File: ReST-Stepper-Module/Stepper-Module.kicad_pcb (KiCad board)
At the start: 2 copper layers, 46 x 32.2 mm, 13 parts, among them P1 CONN_02X10, P2 CONN_01X04, P3 CONN_01X04, P4 CONN_01X04, P5 CONN_01X04, P6 CONN_02X03, P7 CONN_02X03, U1 POLOLU_A4988, U2 POLOLU_A4988

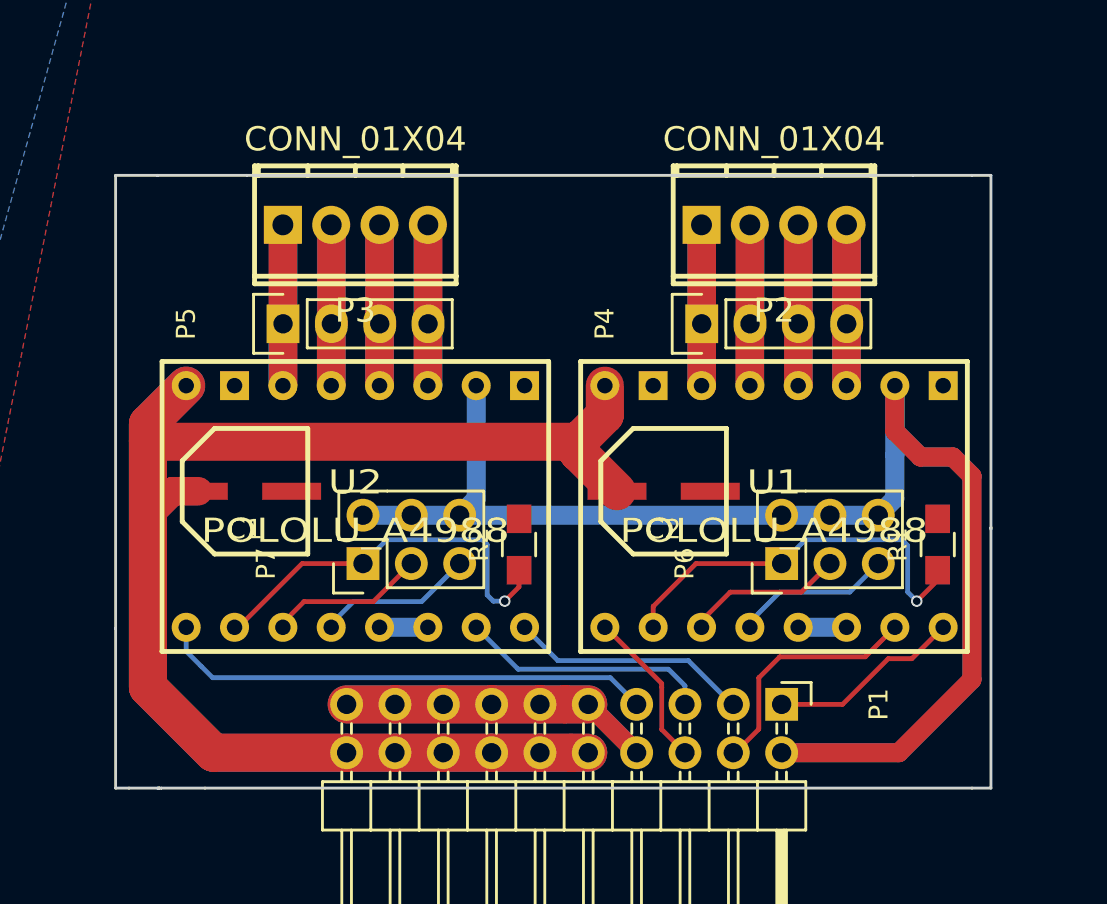
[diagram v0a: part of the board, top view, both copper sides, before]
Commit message: Added Images and PDF's
+ Silkscreening
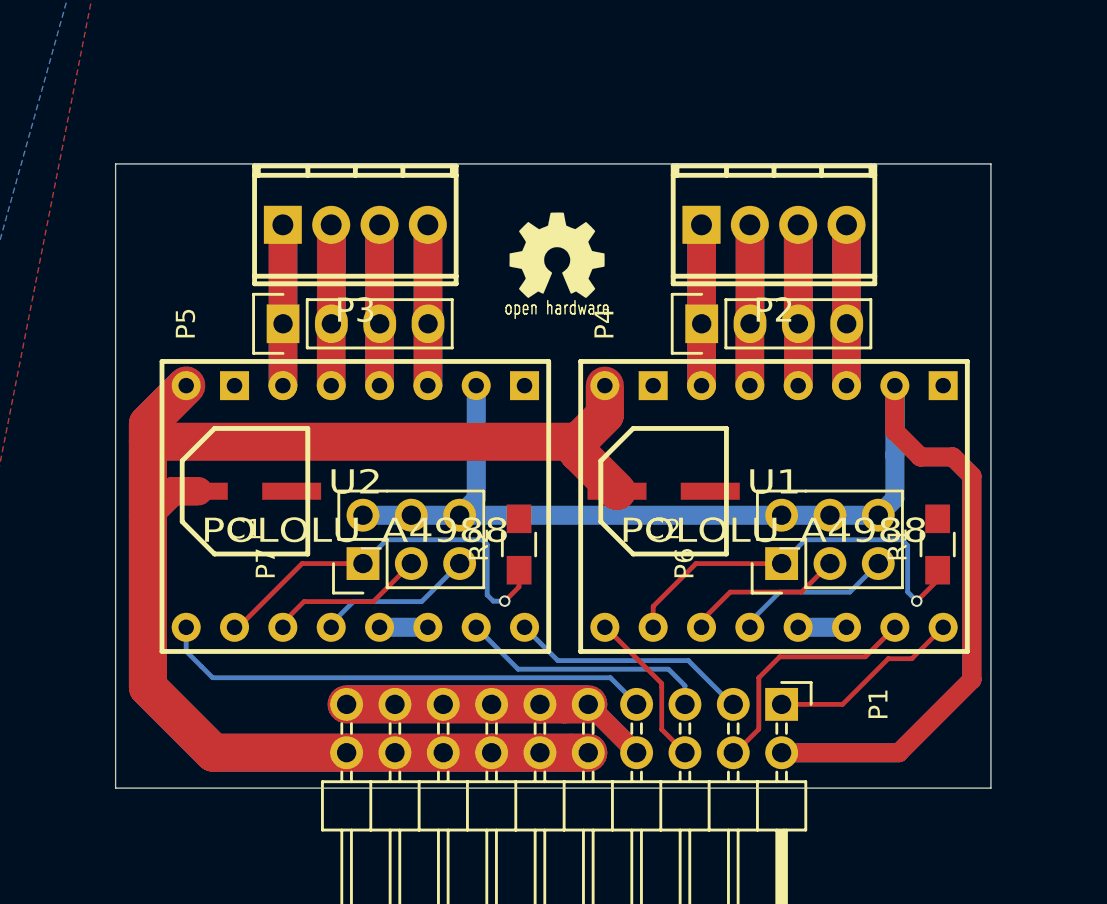
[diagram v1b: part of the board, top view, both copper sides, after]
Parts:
- added G***: LOGO, ReST-Library:STM32, B.Cu at (125.2, 83.6)
- added G***: LOGO, ReST-Library:Logo_silk_OSHW_6x6mm, F.Cu at (125.6, 82.8)
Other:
- board size 46 x 32.2 mm -> 46 x 32.8 mm
- board text added: "ReST32 Stepper Module Rev. A | Test by Straw"

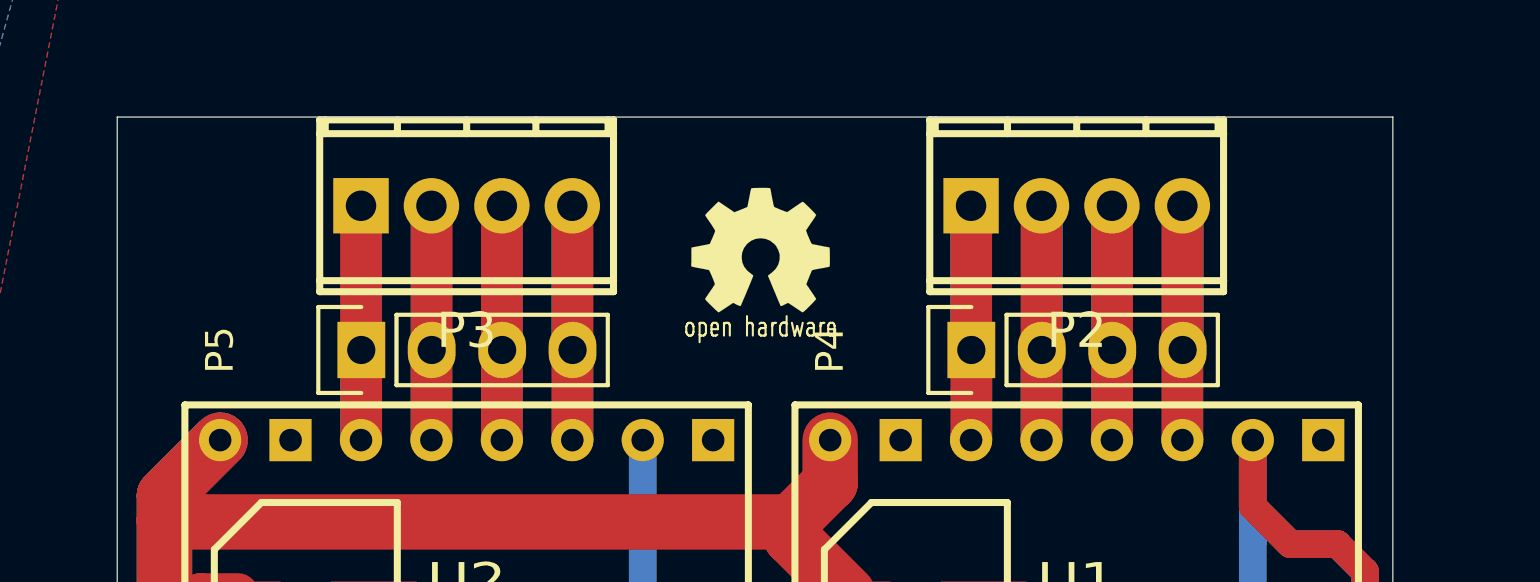
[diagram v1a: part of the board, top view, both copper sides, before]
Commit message: Added Mounting Holes to all Modules
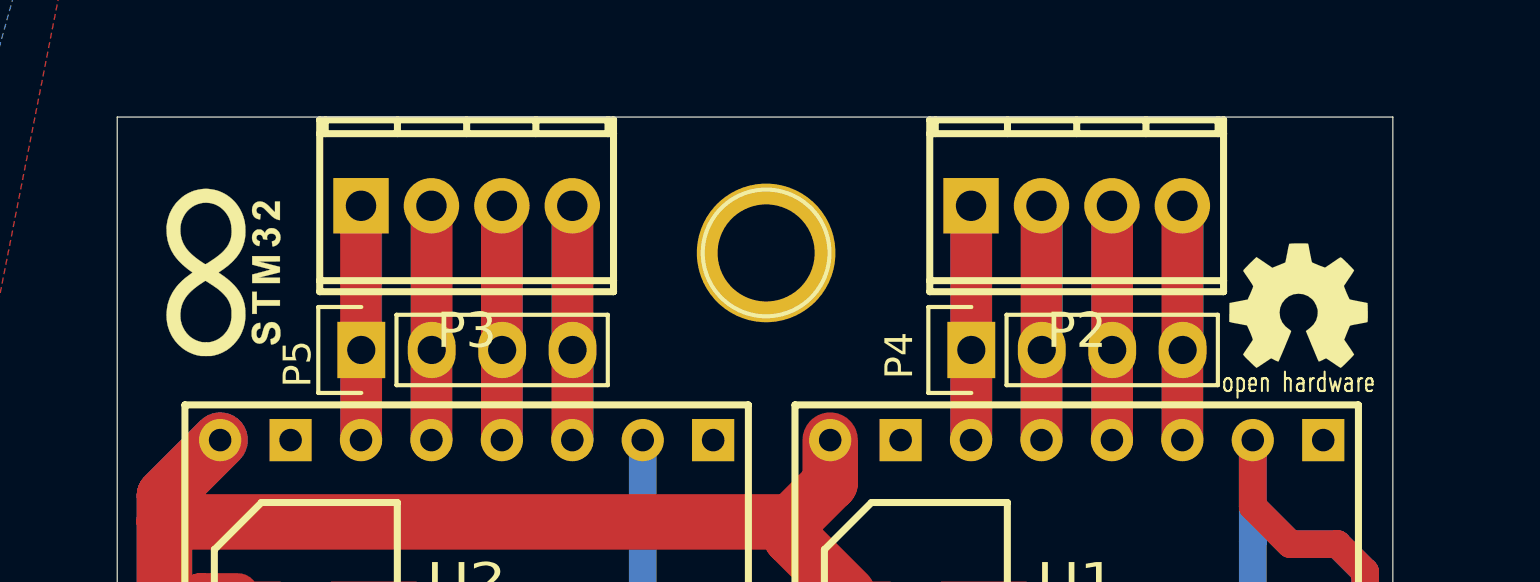
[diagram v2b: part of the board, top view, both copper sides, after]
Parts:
- added ?: 1pin, Connect:1pin, F.Cu at (125.8, 82.9)
- G***: moved to F.Cu
- moved G*** 19.5 mm to (145.0, 84.8)
- moved G*** 18.9 mm to (106.3, 83.6), turned to 90 degrees

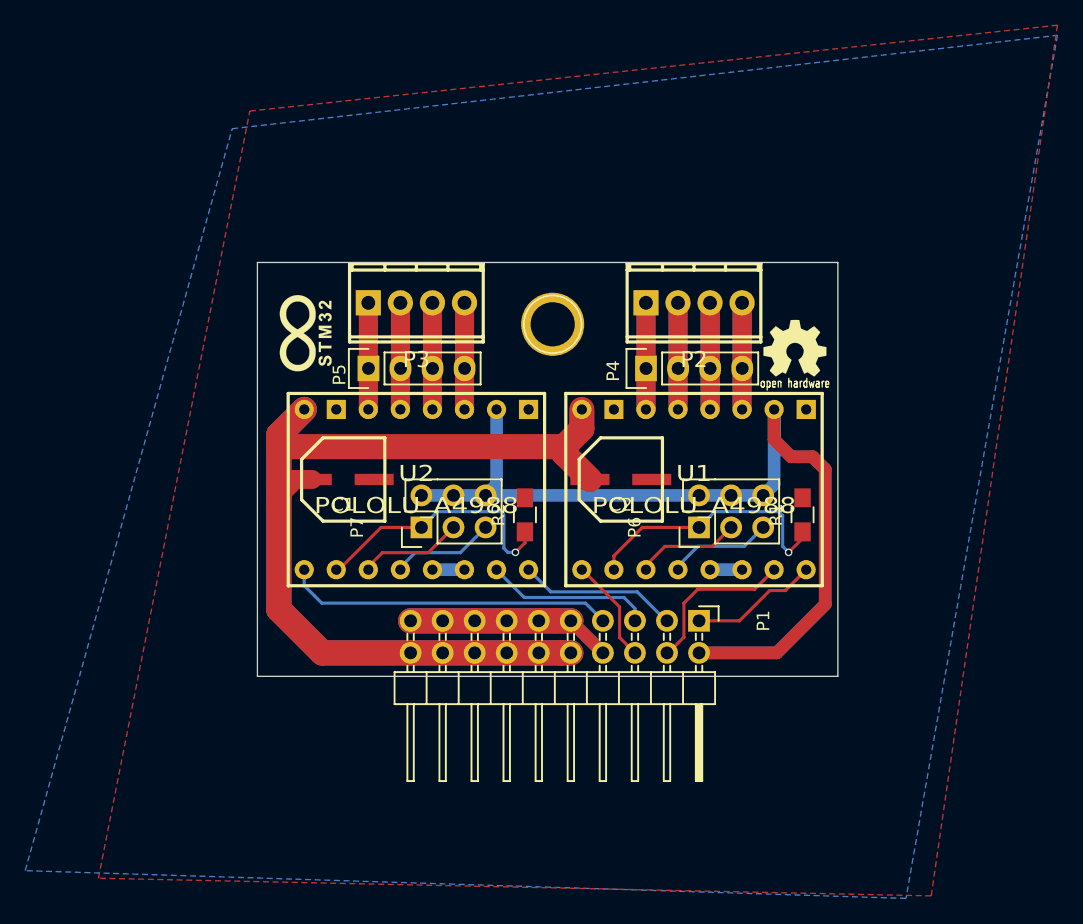
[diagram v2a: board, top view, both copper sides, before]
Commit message: Finally removed all unnecessary Libs and added Heatsink for 5V Regulator
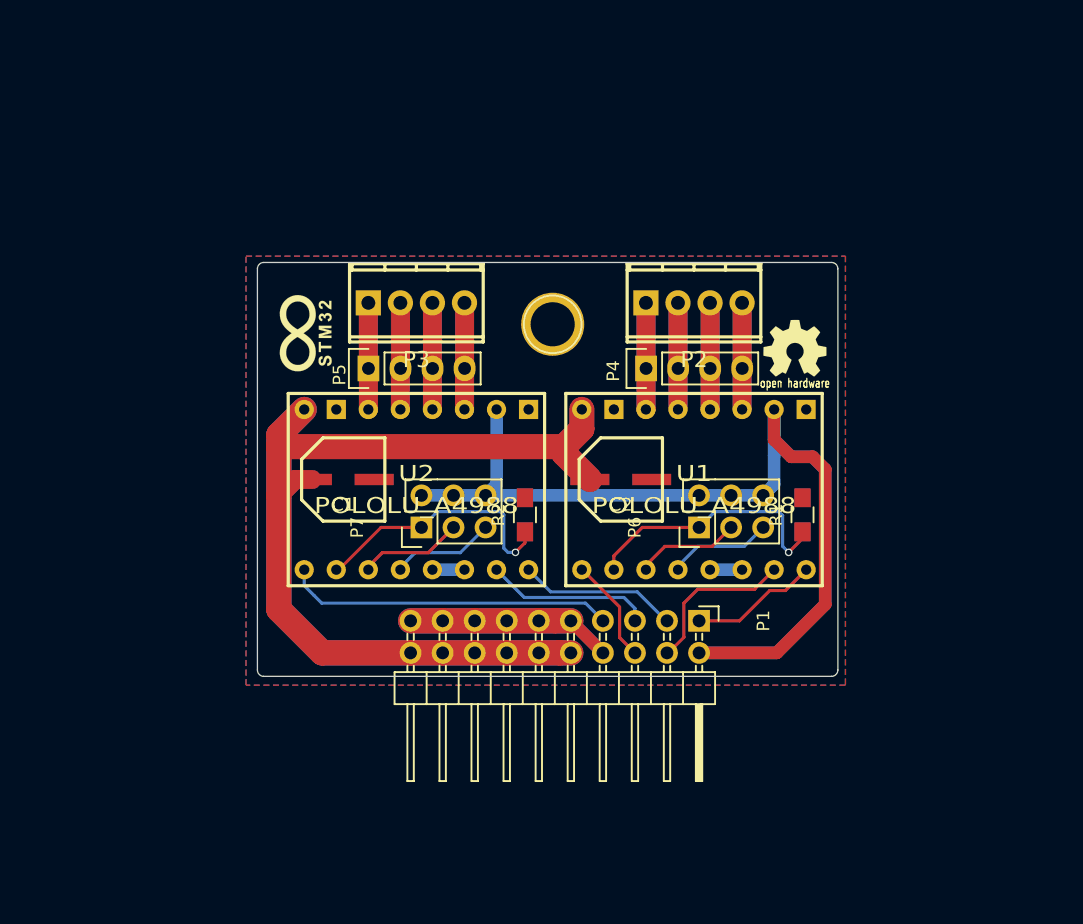
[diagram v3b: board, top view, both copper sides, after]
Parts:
- C1, C2: footprint ok-polcaps-panasonic:CP-PANASONIC-SMT_D8 -> ReST-Library:CP-PANASONIC-SMT_D8
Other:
- outline, holes or cut-outs redrawn
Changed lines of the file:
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@@
     (links 63)
     (no_connects 0)
-    (area 102.394999 77.994999 148.405001 110.805001)
+    (area 84 59.2 165.800001 128.400001)
     (thickness 1.6)
-    (drawings 5)
+    (drawings 9)
     (tracks 205)
     (zones 0)
@@
     (add_net "Net-(U1-Pad13)")
     (add_net "Net-(U2-Pad13)")
-  )
-  (module ok-polcaps-panasonic:CP-PANASONIC-SMT_D8 (layer F.Cu)
-    (at 109.2 95.2)
-    (descr "Panasonic SMT electrolytic capacitor - size code D8")
-    (fp_text reference C1 (at 0 1.99898) (layer F.SilkS)
-      (effects (font (size 1.016 1.016) (thickness 0.254)))
-    )
-    (fp_text value 100uF (at 0 -1.80086) (layer F.SilkS) hide
-      (effects (font (size 1.016 1.016) (thickness 0.254)))
-    )
-    (fp_line (start 3.29946 3.29946) (end 3.29946 -3.29946) (layer F.SilkS) (width 0.254))
-    (fp_line (start 3.29946 -3.29946) (end -1.6002 -3.29946) (layer F.SilkS) (width 0.254))
-    (fp_line (start -1.6002 -3.29946) (end -3.29946 -1.6002) (layer F.SilkS) (width 0.254))
-    (fp_line (start -3.29946 -1.6002) (end -3.29946 1.6002) (layer F.SilkS) (width 0.254))
-    (fp_line (start -3.29946 1.6002) (end -1.6002 3.29946) (layer F.SilkS) (width 0.254))
-    (fp_line (start -1.6002 3.29946) (end 3.29946 3.29946) (layer F.SilkS) (width 0.254))
-    (pad 1 smd rect (at -2.4511 0) (size 3.0988 0.89916) (layers F.Cu F.Paste F.Mask)
-      (net 1 +12V))
-    (pad 2 smd rect (at 2.4511 0) (size 3.0988 0.89916) (layers F.Cu F.Paste F.Mask)
-      (net 2 GND))
-    (model ../../../../../../Users/Matjas/Documents/Git/RepRapSTM32duinoDriver/3D-Models/smd_cap/c_elec_6_3x7_7.wrl
-      (at (xyz 0 0 0))
-      (scale (xyz 1 1 1))
-      (rotate (xyz 0 0 0))
-    )
-  )
-  (module ok-polcaps-panasonic:CP-PANASONIC-SMT_D8 (layer F.Cu)
-    (at 131.2 95.2)
-    (descr "Panasonic SMT electrolytic capacitor - size code D8")
-    (fp_text reference C2 (at 0 1.99898) (layer F.SilkS)
-      (effects (font (size 1.016 1.016) (thickness 0.254)))
-    )
-    (fp_text value 100uF (at 0 -1.80086) (layer F.SilkS) hide
-      (effects (font (size 1.016 1.016) (thickness 0.254)))
-    )
-    (fp_line (start 3.29946 3.29946) (end 3.29946 -3.29946) (layer F.SilkS) (width 0.254))
-    (fp_line (start 3.29946 -3.29946) (end -1.6002 -3.29946) (layer F.SilkS) (width 0.254))
-    (fp_line (start -1.6002 -3.29946) (end -3.29946 -1.6002) (layer F.SilkS) (width 0.254))
-    (fp_line (start -3.29946 -1.6002) (end -3.29946 1.6002) (layer F.SilkS) (width 0.254))
-    (fp_line (start -3.29946 1.6002) (end -1.6002 3.29946) (layer F.SilkS) (width 0.254))
-    (fp_line (start -1.6002 3.29946) (end 3.29946 3.29946) (layer F.SilkS) (width 0.254))
-    (pad 1 smd rect (at -2.4511 0) (size 3.0988 0.89916) (layers F.Cu F.Paste F.Mask)
-      (net 1 +12V))
-    (pad 2 smd rect (at 2.4511 0) (size 3.0988 0.89916) (layers F.Cu F.Paste F.Mask)
-      (net 2 GND))
-    (model ../../../../../../Users/Matjas/Documents/Git/RepRapSTM32duinoDriver/3D-Models/smd_cap/c_elec_6_3x7_7.wrl
-      (at (xyz 0 0 0))
-      (scale (xyz 1 1 1))
-      (rotate (xyz 0 0 0))
-    )
   )
   (module Pin_Headers:Pin_Header_Angled_2x10 (layer F.Cu)
@@
     (pad 1 thru_hole circle (at 0 0) (size 5 5) (drill 3.5) (layers *.Cu *.Mask F.SilkS))
   )
-  (gr_line (start 148.4 78) (end 148.4 110.8) (angle 90) (layer Edge.Cuts) (width 0.01))
-  (gr_line (start 102.4 78) (end 148.4 78) (angle 90) (layer Edge.Cuts) (width 0.01))
-  (gr_line (start 102.4 110.8) (end 102.4 78) (angle 90) (layer Edge.Cuts) (width 0.01))
-  (gr_line (start 148.4 110.8) (end 102.4 110.8) (angle 90) (layer Edge.Cuts) (width 0.01))
+  (module ReST-Library:CP-PANASONIC-SMT_D8 (layer F.Cu)
+    (at 109.2 95.2)
+    (descr "Panasonic SMT electrolytic capacitor - size code D8")
+    (fp_text reference C1 (at 0 1.99898) (layer F.SilkS)
+      (effects (font (size 1.016 1.016) (thickness 0.254)))
+    )
+    (fp_text value 100uF (at 0 -1.80086) (layer F.SilkS) hide
+      (effects (font (size 1.016 1.016) (thickness 0.254)))
+    )
+    (fp_line (start 3.29946 3.29946) (end 3.29946 -3.29946) (layer F.SilkS) (width 0.254))
+    (fp_line (start 3.29946 -3.29946) (end -1.6002 -3.29946) (layer F.SilkS) (width 0.254))
+    (fp_line (start -1.6002 -3.29946) (end -3.29946 -1.6002) (layer F.SilkS) (width 0.254))
+    (fp_line (start -3.29946 -1.6002) (end -3.29946 1.6002) (layer F.SilkS) (width 0.254))
+    (fp_line (start -3.29946 1.6002) (end -1.6002 3.29946) (layer F.SilkS) (width 0.254))
+    (fp_line (start -1.6002 3.29946) (end 3.29946 3.29946) (layer F.SilkS) (width 0.254))
+    (pad 1 smd rect (at -2.4511 0) (size 3.0988 0.89916) (layers F.Cu F.Paste F.Mask)
+      (net 1 +12V))
+    (pad 2 smd rect (at 2.4511 0) (size 3.0988 0.89916) (layers F.Cu F.Paste F.Mask)
+      (net 2 GND))
+  )
+  (module ReST-Library:CP-PANASONIC-SMT_D8 (layer F.Cu)
+    (at 131.2 95.2)
+    (descr "Panasonic SMT electrolytic capacitor - size code D8")
+    (fp_text reference C2 (at 0 1.99898) (layer F.SilkS)
+      (effects (font (size 1.016 1.016) (thickness 0.254)))
+    )
+    (fp_text value 100uF (at 0 -1.80086) (layer F.SilkS) hide
+      (effects (font (size 1.016 1.016) (thickness 0.254)))
+    )
+    (fp_line (start 3.29946 3.29946) (end 3.29946 -3.29946) (layer F.SilkS) (width 0.254))
+    (fp_line (start 3.29946 -3.29946) (end -1.6002 -3.29946) (layer F.SilkS) (width 0.254))
+    (fp_line (start -1.6002 -3.29946) (end -3.29946 -1.6002) (layer F.SilkS) (width 0.254))
+    (fp_line (start -3.29946 -1.6002) (end -3.29946 1.6002) (layer F.SilkS) (width 0.254))
+    (fp_line (start -3.29946 1.6002) (end -1.6002 3.29946) (layer F.SilkS) (width 0.254))
+    (fp_line (start -1.6002 3.29946) (end 3.29946 3.29946) (layer F.SilkS) (width 0.254))
+    (pad 1 smd rect (at -2.4511 0) (size 3.0988 0.89916) (layers F.Cu F.Paste F.Mask)
+      (net 1 +12V))
+    (pad 2 smd rect (at 2.4511 0) (size 3.0988 0.89916) (layers F.Cu F.Paste F.Mask)
+      (net 2 GND))
+  )
+  (gr_arc (start 102.9 78.5) (end 102.4 78.5) (angle 90) (layer Edge.Cuts) (width 0.01))
+  (gr_arc (start 147.9 78.5) (end 147.9 78) (angle 90) (layer Edge.Cuts) (width 0.01))
+  (gr_arc (start 147.9 110.3) (end 148.4 110.3) (angle 90) (layer Edge.Cuts) (width 0.01))
+  (gr_arc (start 102.9 110.3) (end 102.9 110.8) (angle 90) (layer Edge.Cuts) (width 0.01))
+  (gr_line (start 102.4 78.5) (end 102.4 110.3) (angle 90) (layer Edge.Cuts) (width 0.01))
+  (gr_line (start 147.9 78) (end 102.9 78) (angle 90) (layer Edge.Cuts) (width 0.01))
+  (gr_line (start 148.4 110.3) (end 148.4 78.5) (angle 90) (layer Edge.Cuts) (width 0.01))
+  (gr_line (start 102.9 110.8) (end 147.9 110.8) (angle 90) (layer Edge.Cuts) (width 0.01))
   (gr_text "ReST32 Stepper Module\nRev. A | Test\nby Straw" (at 129.8 94) (layer B.SilkS)
     (effects (font (size 1 1) (thickness 0.2)) (justify mirror))
@@
     (polygon
       (pts
-        (xy 101.8 66) (xy 165.8 59.2) (xy 155.8 128.2) (xy 89.8 126.8)
+        (xy 149 111.5) (xy 101.5 111.5) (xy 101.5 77.5) (xy 149 77.5) (xy 149 111.5)
       )
     )
@@
     (polygon
       (pts
-        (xy 100.4 67.4) (xy 165.8 60) (xy 153.8 128.4) (xy 84 126.2)
+        (xy 149 111.5) (xy 101.5 111.5) (xy 101.5 77.5) (xy 149 77.5)
       )
     )
